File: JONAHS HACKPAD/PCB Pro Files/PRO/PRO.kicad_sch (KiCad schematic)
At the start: 25 parts, among them SW2 SW_Push, SW3 SW_Push, SW4 SW_Push, SW5 SW_Push, U1 MOUDLE-SEEEDUINO-XIAO, U2 OLED_0.91_128x32

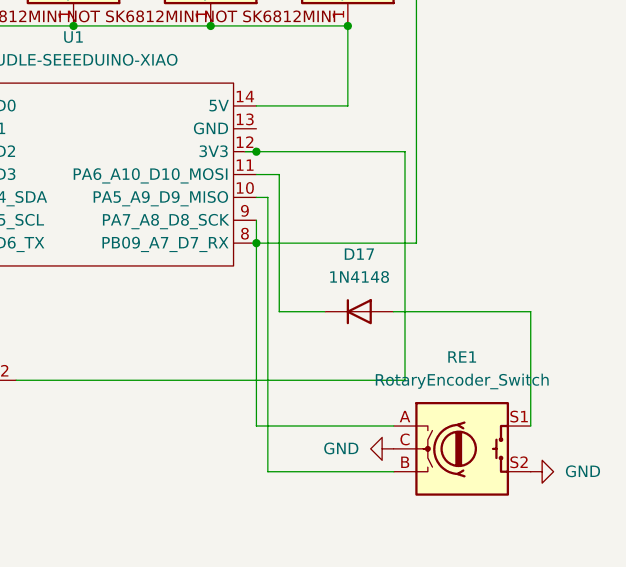
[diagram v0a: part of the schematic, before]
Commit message: move stuff to root cad and diode fix
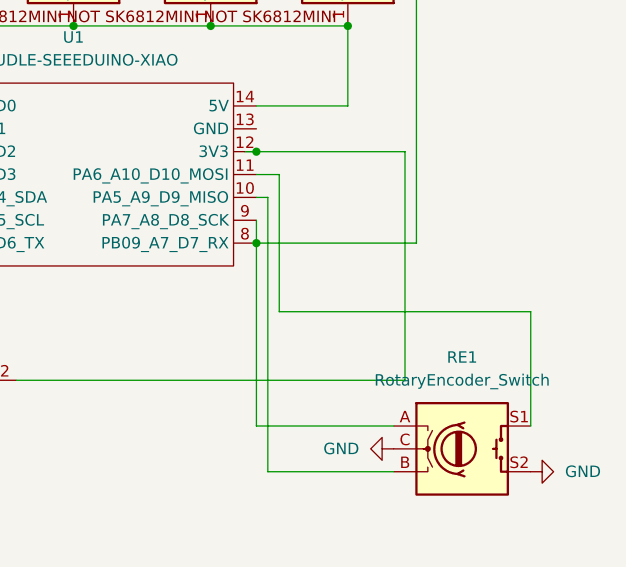
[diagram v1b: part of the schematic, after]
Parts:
- removed D17: 1N4148, Diode_SMD:D_SOD-123, symbol Diode:1N4148
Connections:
- net at U1.11 (PA6_A10_D10_MOSI): now also RE1.S1
- net at D10.1 (DOUT): now also D11.1 (DOUT), D12.1 (DOUT), D13.1 (DOUT), D14.1 (DOUT), D15.1 (DOUT), D16.1 (DOUT), D6.1 (DOUT), D7.1 (DOUT), D8.1 (DOUT), D9.1 (DOUT), U1.14 (5V)
- now unconnected: D16.1 (DOUT)
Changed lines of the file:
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@@
 	(wire
 		(pts
-			(xy 204.47 99.06) (xy 199.39 99.06)
+			(xy 199.39 99.06) (xy 227.33 99.06)
 		)
 		(stroke
@@
 	(wire
 		(pts
-			(xy 227.33 99.06) (xy 212.09 99.06)
-		)
-		(stroke
-			(width 0)
-			(type default)
-		)
-	)
-	(wire
-		(pts
 			(xy 132.08 67.31) (xy 146.05 67.31)
 		)
@@
 		)
 	)
-	(symbol
-		(lib_id "Diode:1N4148")
-		(at 208.28 99.06 0)
-		(unit 1)
-		(exclude_from_sim no)
-		(in_bom yes)
-		(on_board yes)
-		(dnp no)
-		(fields_autoplaced yes)
-		(property "Reference" "D17"
-			(at 208.28 92.71 0)
-			(effects
-				(font
-					(size 1.27 1.27)
-				)
-			)
-		)
-		(property "Value" "1N4148"
-			(at 208.28 95.25 0)
-			(effects
-				(font
-					(size 1.27 1.27)
-				)
-			)
-		)
-		(property "Footprint" "Diode_SMD:D_SOD-123"
-			(at 208.28 99.06 0)
-			(effects
-				(font
-					(size 1.27 1.27)
-				)
-				(hide yes)
-			)
-		)
-		(property "Datasheet" "https://assets.nexperia.com/documents/data-sheet/1N4148_1N4448.pdf"
-			(at 208.28 99.06 0)
-			(effects
-				(font
-					(size 1.27 1.27)
-				)
-				(hide yes)
-			)
-		)
-		(property "Description" "100V 0.15A standard switching diode, DO-35"
-			(at 208.28 99.06 0)
-			(effects
-				(font
-					(size 1.27 1.27)
-				)
-				(hide yes)
-			)
-		)
-		(property "Sim.Device" "D"
-			(at 208.28 99.06 0)
-			(effects
-				(font
-					(size 1.27 1.27)
-				)
-				(hide yes)
-			)
-		)
-		(property "Sim.Pins" "1=K 2=A"
-			(at 208.28 99.06 0)
-			(effects
-				(font
-					(size 1.27 1.27)
-				)
-				(hide yes)
-			)
-		)
-		(pin "1"
-		)
-		(pin "2"
-		)
-		(instances
-			(project "HACK PAD!"
-				(path "/a709c780-9f71-42cb-8f66-67c5b8585a22"
-					(reference "D17")
-					(unit 1)
-				)
-			)
-		)
-	)
